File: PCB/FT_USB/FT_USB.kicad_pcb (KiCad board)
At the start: 2 copper layers, 25 x 25 mm, 2 parts, among them CON1 USB_B, CON2 Conn_01x03

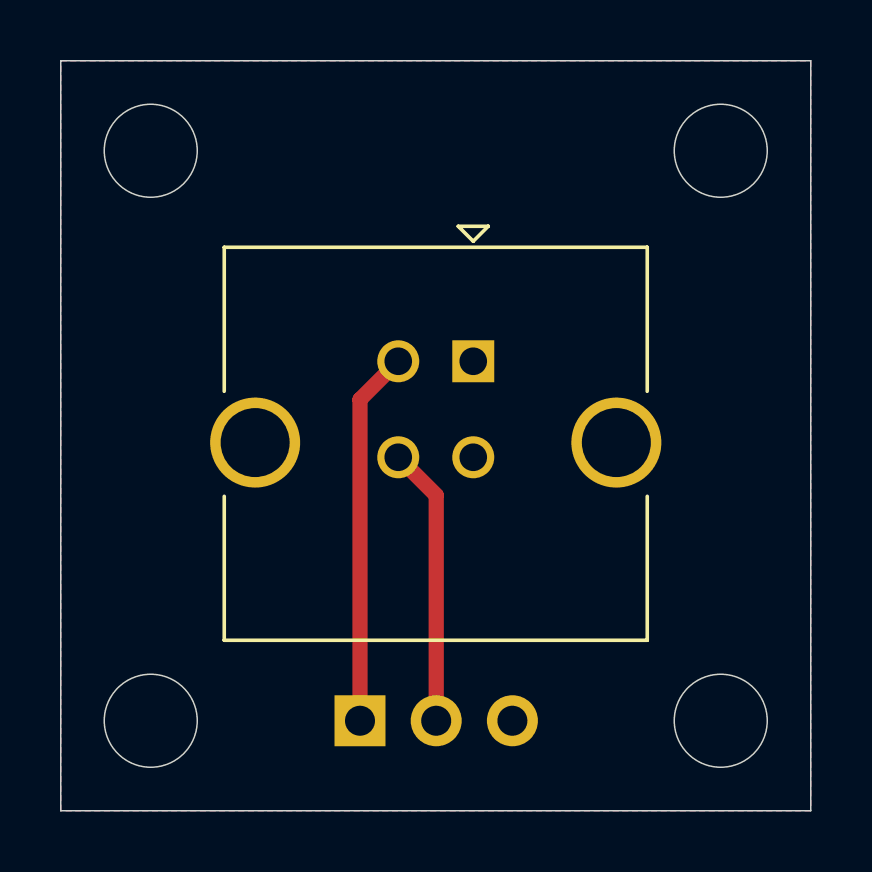
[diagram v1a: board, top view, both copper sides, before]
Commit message: .gitignore update, USB update
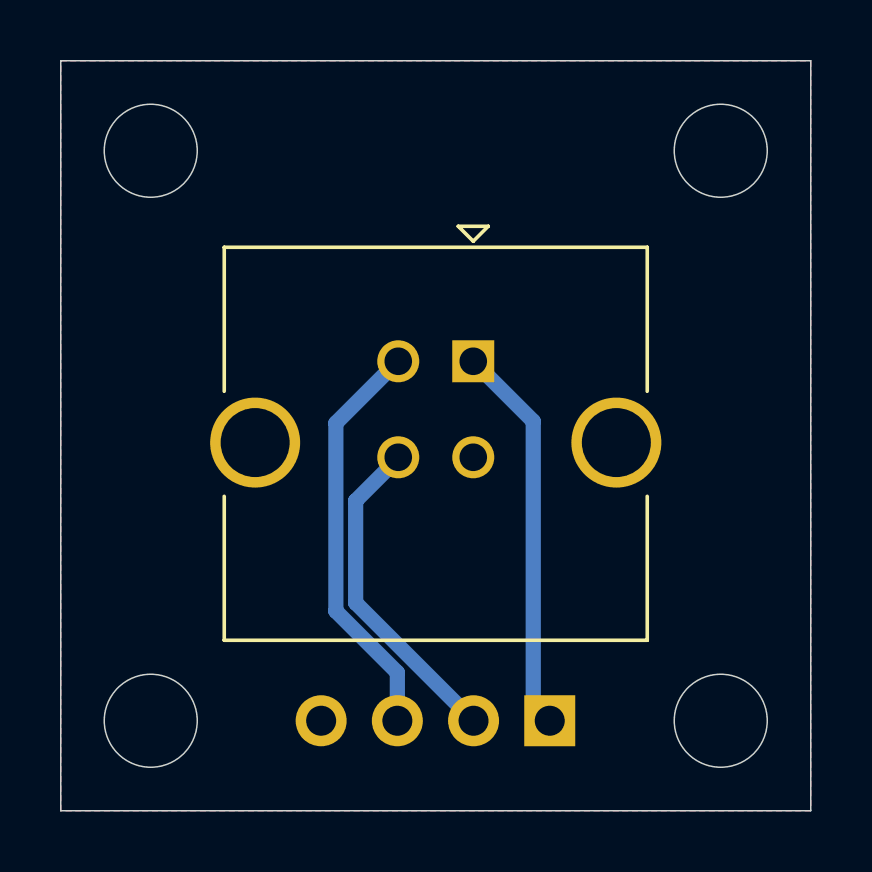
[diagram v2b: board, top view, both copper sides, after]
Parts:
- removed CON2: Conn_01x03, Connector_PinHeader_2.54mm:PinHeader_1x03_P2.54mm_Vertical
- added J1: Conn_01x04, Connector_PinHeader_2.54mm:PinHeader_1x04_P2.54mm_Vertical, B.Cu at (116.3, 122.0)
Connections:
- CON1 pad 1: unconnected-(CON1-VBUS-Pad1) -> Net-(CON1-VBUS)
- CON1 pad 2: Net-(CON1-D-) -> /USB_D-
- CON1 pad 3: Net-(CON1-D+) -> /USB_D+
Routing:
- net /USB_D-: track 0.00 -> 13.7 mm
- net Net-(CON1-VBUS): track 0.00 -> 13.0 mm
- net Net-(CON1-D-): track 12.5 -> 0.00 mm
- net /USB_D+: track 0.00 -> 11.0 mm
- net Net-(CON1-D+): track 9.31 -> 0.00 mm
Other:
- board text added: "D+"
- board text added: "D-"
- board text added: "GND"
- board text added: "VCC"
- board text removed: "GND D+ D-"

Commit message: panelization
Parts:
- renumbered CON1 to CON301, J1 to CON302
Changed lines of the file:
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@@
 	)
 	(net 0 "")
-	(net 1 "Net-(CON1-VBUS)")
+	(net 1 "Net-(CON301-VBUS)")
 	(net 2 "GND")
 	(net 3 "/USB_D-")
@@
 		(descr "http://www.mouser.com/ds/2/418/NG_CD_5787834_A4-669110.pdf")
 		(tags "USB_B USB B vertical female connector")
-		(property "Reference" "CON1"
+		(property "Reference" "CON301"
 			(at -5.8 -4.55 0)
 			(layer "F.SilkS")
@@
 		)
 		(property "URL" "https://www.gme.cz/v/1502411/connfly-ds1099-01-wn0-konektor-usb-b-20"
+			(at 0 0 0)
+			(unlocked yes)
+			(layer "F.Fab")
+			(hide yes)
+			(effects
+				(font
+					(size 1 1)
+					(thickness 0.15)
+				)
+			)
+		)
+		(property "Accept alternative part" ""
 			(at 0 0 0)
 			(unlocked yes)
@@
 			(layers "*.Cu" "*.Mask")
 			(remove_unused_layers no)
-			(net 1 "Net-(CON1-VBUS)")
+			(net 1 "Net-(CON301-VBUS)")
 			(pinfunction "VBUS")
 			(pintype "power_out")
@@
 		(descr "Through hole straight pin header, 1x04, 2.54mm pitch, single row")
 		(tags "Through hole pin header THT 1x04 2.54mm single row")
-		(property "Reference" "J1"
-			(at 0 2.33 270)
+		(property "Reference" "CON302"
+			(at 0 2.33 -90)
 			(layer "B.SilkS")
 			(hide yes)
@@
 		)
 		(property "Value" "Conn_01x04"
-			(at 0 -9.95 270)
+			(at 0 -9.95 -90)
 			(layer "B.Fab")
 			(hide yes)
@@
 			)
 		)
-		(property "Datasheet" ""
+		(property "Datasheet" "https://img.gme.cz/files/eshop_data/eshop_data/5/800-170/dsh.800-170.1.pdf"
 			(at 0 0 -90)
 			(unlocked yes)
@@
 				(font
 					(size 1.27 1.27)
+				)
+				(justify mirror)
+			)
+		)
+		(property "Accept alternative part" ""
+			(at 0 0 90)
+			(unlocked yes)
+			(layer "B.Fab")
+			(hide yes)
+			(effects
+				(font
+					(size 1 1)
+					(thickness 0.15)
+				)
+				(justify mirror)
+			)
+		)
+		(property "Assemble" "NO"
+			(at 0 0 90)
+			(unlocked yes)
+			(layer "B.Fab")
+			(hide yes)
+			(effects
+				(font
+					(size 1 1)
+					(thickness 0.15)
+				)
+				(justify mirror)
+			)
+		)
+		(property "Supplier" "GME"
+			(at 0 0 90)
+			(unlocked yes)
+			(layer "B.Fab")
+			(hide yes)
+			(effects
+				(font
+					(size 1 1)
+					(thickness 0.15)
+				)
+				(justify mirror)
+			)
+		)
+		(property "Supplier no." "800-170"
+			(at 0 0 90)
+			(unlocked yes)
+			(layer "B.Fab")
+			(hide yes)
+			(effects
+				(font
+					(size 1 1)
+					(thickness 0.15)
+				)
+				(justify mirror)
+			)
+		)
+		(property "URL" "https://www.gme.cz/v/1497969/kls-psh02-04pg-konektor-vidlice-roztec-254mm-1x4piny-prima-do-dps"
+			(at 0 0 90)
+			(unlocked yes)
+			(layer "B.Fab")
+			(hide yes)
+			(effects
+				(font
+					(size 1 1)
+					(thickness 0.15)
 				)
 				(justify mirror)
@@
 			(layers "*.Cu" "*.Mask")
 			(remove_unused_layers no)
-			(net 1 "Net-(CON1-VBUS)")
+			(net 1 "Net-(CON301-VBUS)")
 			(pinfunction "Pin_1")
 			(pintype "passive")
